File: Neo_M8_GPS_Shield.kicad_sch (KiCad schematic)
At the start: 37 parts, among them J10 Conn_01x01_Male, J11 Conn_01x02_Male, J12 Conn_01x01_Male, J13 Conn_01x01_Male, P1 USB_C_Plug_USB2.0, Q1 MMBT3904, SW1 SW_Push, SW2 SW_DIP_x01, SW3 SW_DIP_x01, U1 NEO-M8Q, U2 AZ1117-3.3, U3 74LVC1G18, U4 74LS157

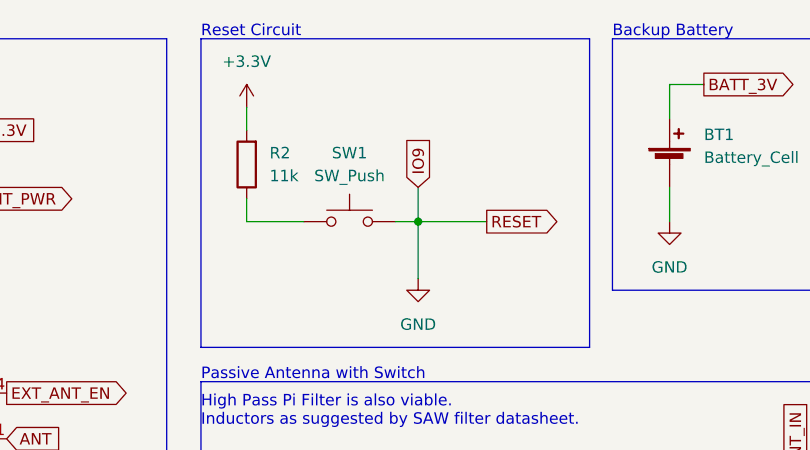
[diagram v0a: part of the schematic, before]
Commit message: reset circuit changed to pull down
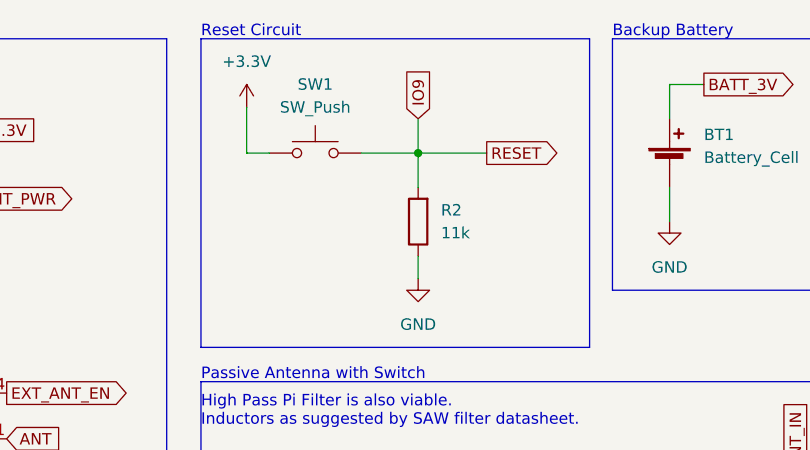
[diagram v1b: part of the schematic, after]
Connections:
- net +3V3: now also SW1.1; no longer R2.2
- net GND: now also R2.1; no longer SW1.2, U1.8 (~{RESET})
- new net IO9: R2.2, SW1.2, U1.8 (~{RESET})
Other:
- moved on the sheet: SW1
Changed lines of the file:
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@@
   (junction (at 205.74 115.57) (diameter 0) (color 0 0 0 0)
   )
-  (junction (at 111.76 35.56) (diameter 0) (color 0 0 0 0)
+  (junction (at 111.76 27.94) (diameter 0) (color 0 0 0 0)
   )
   (no_connect (at 266.7 88.9))
@@
     (stroke (width 0) (type default) (color 0 0 0 0))
   )
-  (wire (pts (xy 111.76 35.56) (xy 119.38 35.56))
+  (wire (pts (xy 111.76 27.94) (xy 119.38 27.94))
     (stroke (width 0) (type default) (color 0 0 0 0))
   )
@@
     (stroke (width 0) (type default) (color 0 0 0 0))
   )
-  (wire (pts (xy 92.71 35.56) (xy 99.06 35.56))
+  (wire (pts (xy 92.71 27.94) (xy 95.25 27.94))
     (stroke (width 0) (type default) (color 0 0 0 0))
   )
@@
     (stroke (width 0) (type default) (color 0 0 0 0))
   )
-  (wire (pts (xy 111.76 31.75) (xy 111.76 35.56))
+  (wire (pts (xy 111.76 24.13) (xy 111.76 27.94))
     (stroke (width 0) (type default) (color 0 0 0 0))
   )
@@
     (stroke (width 0) (type default) (color 0 0 0 0))
   )
-  (wire (pts (xy 92.71 22.86) (xy 92.71 25.4))
-    (stroke (width 0) (type default) (color 0 0 0 0))
-  )
   (polyline (pts (xy 184.15 102.87) (xy 226.06 102.87))
     (stroke (width 0) (type default) (color 0 0 0 0))
@@
     (stroke (width 0) (type default) (color 0 0 0 0))
   )
-  (wire (pts (xy 111.76 35.56) (xy 111.76 41.91))
+  (wire (pts (xy 111.76 27.94) (xy 111.76 31.75))
     (stroke (width 0) (type default) (color 0 0 0 0))
   )
@@
     (stroke (width 0) (type default) (color 0 0 0 0))
   )
+  (wire (pts (xy 111.76 39.37) (xy 111.76 41.91))
+    (stroke (width 0) (type default) (color 0 0 0 0))
+  )
   (polyline (pts (xy 227.33 46.99) (xy 227.33 15.24))
     (stroke (width 0) (type default) (color 0 0 0 0))
   )
-  (wire (pts (xy 92.71 35.56) (xy 92.71 33.02))
+  (wire (pts (xy 92.71 22.86) (xy 92.71 27.94))
     (stroke (width 0) (type default) (color 0 0 0 0))
   )
@@
     (stroke (width 0) (type default) (color 0 0 0 0))
   )
-  (wire (pts (xy 109.22 35.56) (xy 111.76 35.56))
+  (wire (pts (xy 105.41 27.94) (xy 111.76 27.94))
     (stroke (width 0) (type default) (color 0 0 0 0))
   )
@@
     )
   )
-  (global_label "IO9" (shape input) (at 111.76 31.75 90) (fields_autoplaced)
-    (effects (font (size 1.27 1.27)) (justify left))
-    (property "Intersheet References" "${INTERSHEET_REFS}" (id 0) (at 111.6806 26.1921 90)
+  (global_label "IO9" (shape input) (at 111.76 24.13 90) (fields_autoplaced)
+    (effects (font (size 1.27 1.27)) (justify left))
+    (property "Intersheet References" "${INTERSHEET_REFS}" (id 0) (at 111.6806 18.5721 90)
       (effects (font (size 1.27 1.27)) (justify left) hide)
     )
@@
     )
   )
-  (global_label "RESET" (shape output) (at 119.38 35.56 0) (fields_autoplaced)
-    (effects (font (size 1.27 1.27)) (justify left))
-    (property "Intersheet References" "${INTERSHEET_REFS}" (id 0) (at 127.5383 35.4806 0)
+  (global_label "RESET" (shape output) (at 119.38 27.94 0) (fields_autoplaced)
+    (effects (font (size 1.27 1.27)) (justify left))
+    (property "Intersheet References" "${INTERSHEET_REFS}" (id 0) (at 127.5383 27.8606 0)
       (effects (font (size 1.27 1.27)) (justify left) hide)
     )
@@
     (pin "2")
   )
-  (symbol (lib_id "Switch:SW_Push") (at 104.14 35.56 0) (unit 1)
-    (in_bom yes) (on_board yes) (fields_autoplaced)
-    (property "Reference" "SW1" (id 0) (at 104.14 27.94 0))
-    (property "Value" "SW_Push" (id 1) (at 104.14 30.48 0))
-    (property "Footprint" "" (id 2) (at 104.14 30.48 0)
-      (effects (font (size 1.27 1.27)) hide)
-    )
-    (property "Datasheet" "~" (id 3) (at 104.14 30.48 0)
-      (effects (font (size 1.27 1.27)) hide)
-    )
-    (pin "1")
-    (pin "2")
-  )
-  (symbol (lib_id "Device:R") (at 92.71 29.21 180) (unit 1)
-    (in_bom yes) (on_board yes) (fields_autoplaced)
-    (property "Reference" "R2" (id 0) (at 95.25 27.9399 0)
-      (effects (font (size 1.27 1.27)) (justify right))
-    )
-    (property "Value" "11k" (id 1) (at 95.25 30.4799 0)
-      (effects (font (size 1.27 1.27)) (justify right))
-    )
-    (property "Footprint" "" (id 2) (at 94.488 29.21 90)
-      (effects (font (size 1.27 1.27)) hide)
-    )
-    (property "Datasheet" "~" (id 3) (at 92.71 29.21 0)
+  (symbol (lib_id "Switch:SW_Push") (at 100.33 27.94 0) (unit 1)
+    (in_bom yes) (on_board yes) (fields_autoplaced)
+    (property "Reference" "SW1" (id 0) (at 100.33 20.32 0))
+    (property "Value" "SW_Push" (id 1) (at 100.33 22.86 0))
+    (property "Footprint" "" (id 2) (at 100.33 22.86 0)
+      (effects (font (size 1.27 1.27)) hide)
+    )
+    (property "Datasheet" "~" (id 3) (at 100.33 22.86 0)
       (effects (font (size 1.27 1.27)) hide)
     )
@@
     (pin "1")
   )
+  (symbol (lib_id "Device:R") (at 111.76 35.56 180) (unit 1)
+    (in_bom yes) (on_board yes) (fields_autoplaced)
+    (property "Reference" "R2" (id 0) (at 114.3 34.2899 0)
+      (effects (font (size 1.27 1.27)) (justify right))
+    )
+    (property "Value" "11k" (id 1) (at 114.3 36.8299 0)
+      (effects (font (size 1.27 1.27)) (justify right))
+    )
+    (property "Footprint" "" (id 2) (at 113.538 35.56 90)
+      (effects (font (size 1.27 1.27)) hide)
+    )
+    (property "Datasheet" "~" (id 3) (at 111.76 35.56 0)
+      (effects (font (size 1.27 1.27)) hide)
+    )
+    (pin "1")
+    (pin "2")
+  )
   (symbol (lib_id "power:GND") (at 39.37 123.19 0) (unit 1)

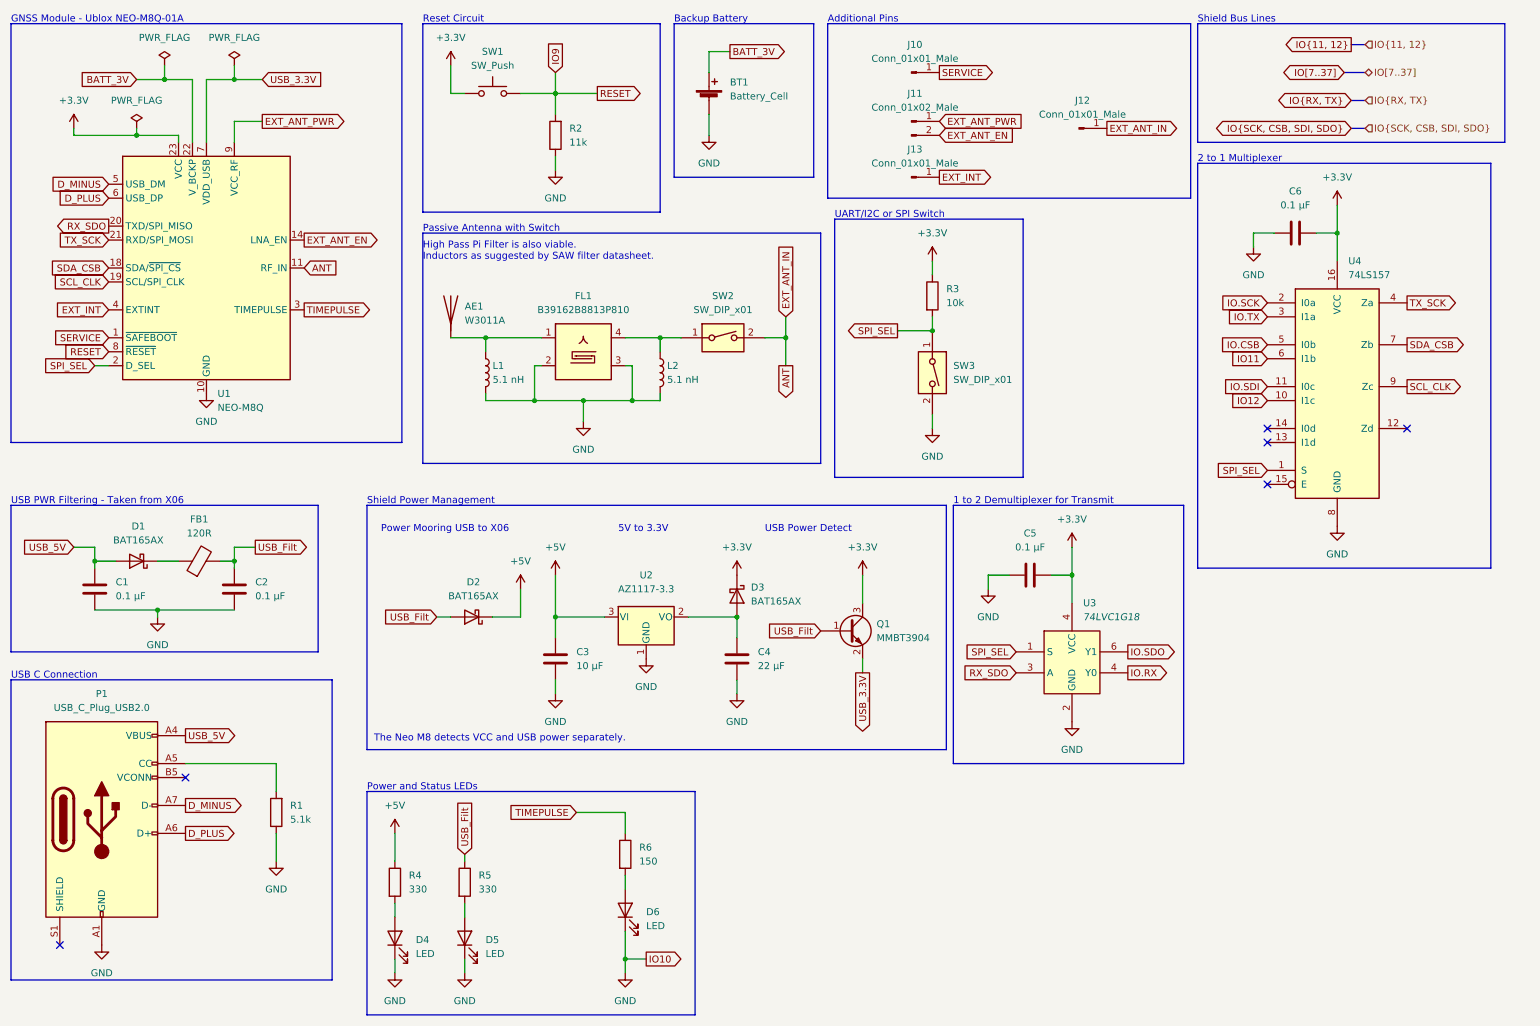
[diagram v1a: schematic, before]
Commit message: simplified power management components
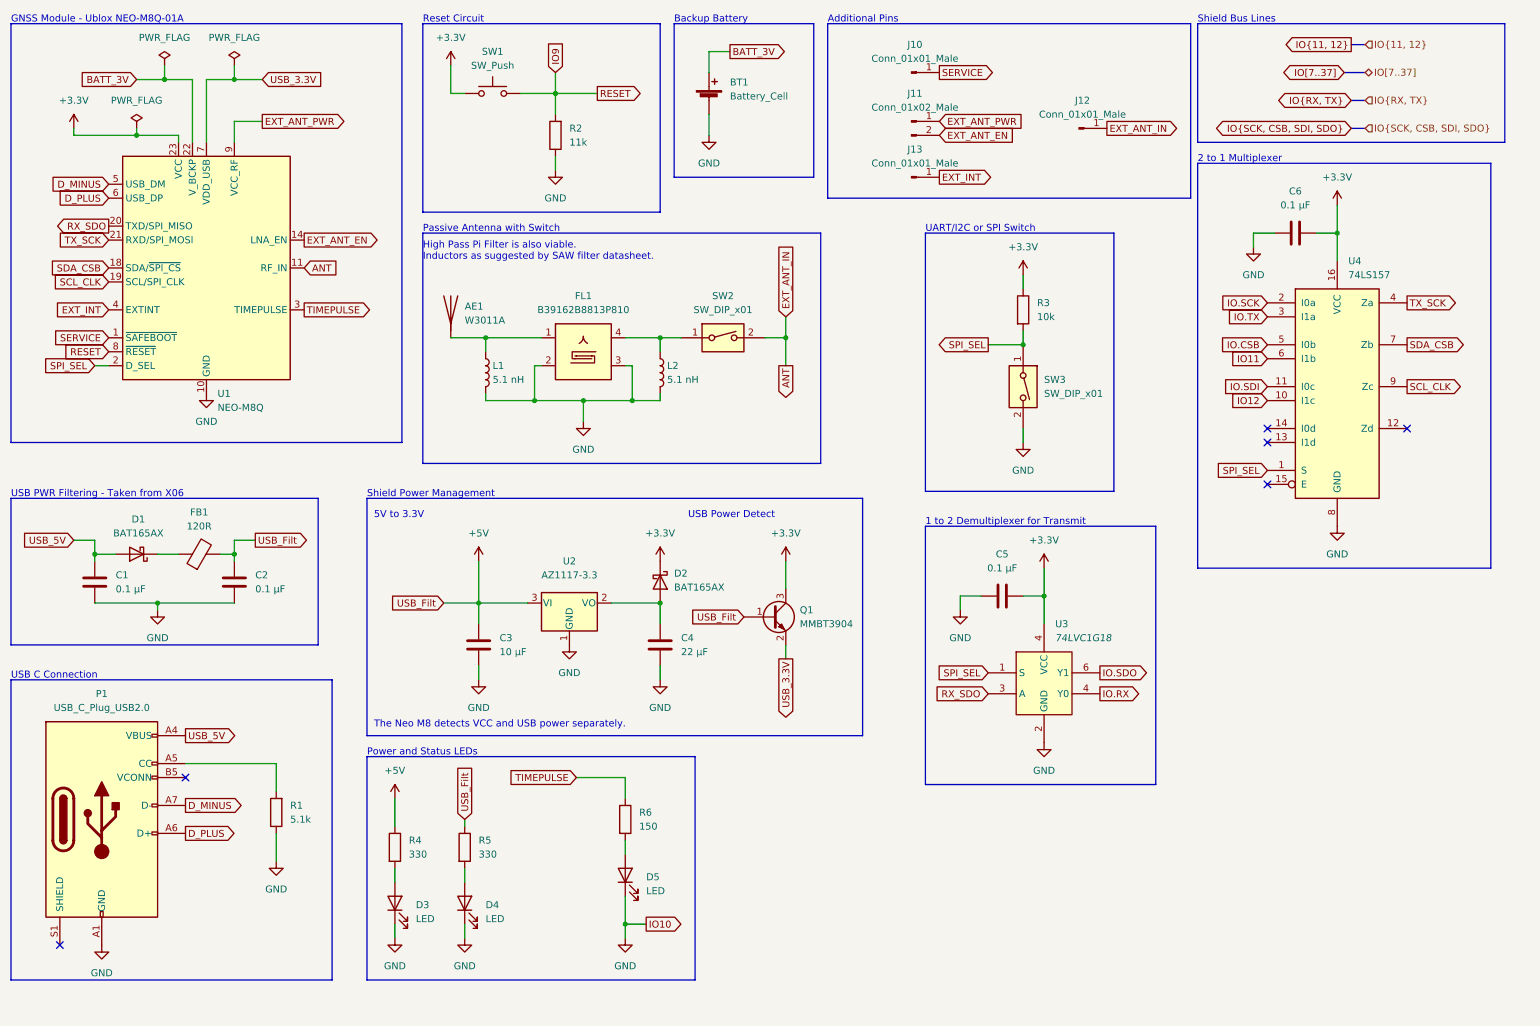
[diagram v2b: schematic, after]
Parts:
- removed D2: BAT165AX, Diode_SMD:D_0402_1005Metric, symbol Device:D_Schottky
- renumbered D3 to D2, D4 to D3, D5 to D4, D6 to D5
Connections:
- net USB_Filt is gone; now on net +5V: C2.1, FB1.2, Q1.1 (B), R5.1
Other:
- note removed: "Power Mooring USB to X06"
- moved on the sheet: C1, C2, C3, C4, C5, D1, D2, D3, D4, D5, FB1, Q1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

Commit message: pcb v1 design done, silkscreen still needs work
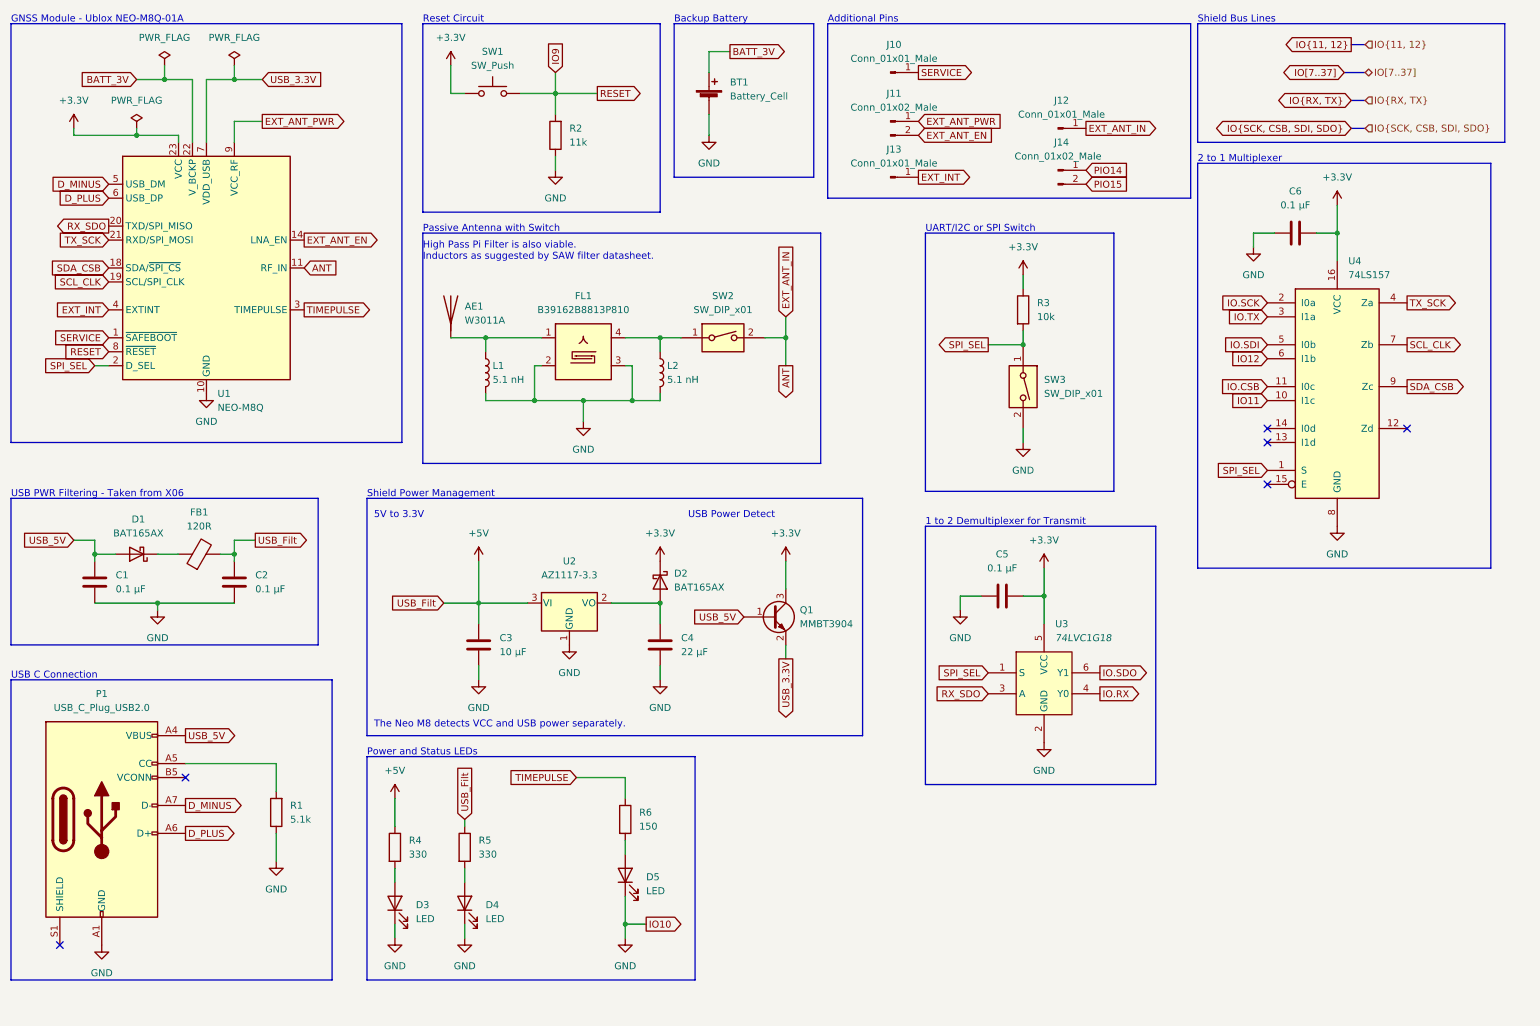
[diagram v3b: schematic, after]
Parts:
- added J14: Conn_01x02_Male, symbol Connector:Conn_01x02_Male
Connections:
- net +3V3: now also U3.5 (VCC); no longer U3.4 (Y0)
- net +5V: no longer Q1.1 (B)
- net IO.CSB: now also U4.11 (I0c); no longer U4.5 (I0b)
- net IO.SDI: now also U4.5 (I0b); no longer U4.11 (I0c)
- net IO11: now also U4.10 (I1c); no longer U4.6 (I1b)
- net IO12: now also U4.6 (I1b); no longer U4.10 (I1c)
- net SCL_CLK: now also U4.7 (Zb); no longer U4.9 (Zc)
- net SDA_CSB: now also U4.9 (Zc); no longer U4.7 (Zb)
- net USB_5V: now also Q1.1 (B)
- new net PIO14: J14.1 (Pin_1)
- new net PIO15: J14.2 (Pin_2)
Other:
- moved on the sheet: J10, J11, J12, J13
